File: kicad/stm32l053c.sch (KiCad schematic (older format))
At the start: 29 parts, among them P1 SWD, SW1 SW_PUSH, SW2 SW_PUSH, SW3 SW_PUSH, U1 STM32L053C8_LQFP48, U2 TLV61225, Y1 Crystal

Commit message: Some footprints
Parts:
- C10, C11, C5: footprint (none) -> Capacitors_SMD:C_0805_HandSoldering
- C8, C9: footprint Capacitors_SMD:C_0805_HandSoldering -> Capacitors_SMD:C_0603_HandSoldering
- L1: footprint (none) -> Inductors:Inductor_1212
- LS1: renamed from LS?; footprint (none) -> Resistors_SMD:R_0805_HandSoldering
- P1: footprint Pin_Headers:Pin_Header_Straight_1x06 -> Pin_Headers:Pin_Header_Straight_1x05
- Q1: renamed from Q?; footprint (none) -> TO_SOT_Packages_SMD:SOT-23_Handsoldering
- R3, R4, R5: footprint (none) -> Resistors_SMD:R_0805_HandSoldering
- R6: renamed from R?; footprint (none) -> Resistors_SMD:R_0805_HandSoldering
- U2: footprint (none) -> TO_SOT_Packages_SMD:SC-70-6
- Y1: footprint (none) -> Crystals:ABM3
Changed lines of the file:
@@
 $EndDescr
 $Comp
-L Earth #PWR24
+L Earth #PWR26
 U 1 1 58021BE1
 P 4900 7200
-F 0 "#PWR24" H 4900 6950 50  0001 C CNN
+F 0 "#PWR26" H 4900 6950 50  0001 C CNN
 F 1 "Earth" H 4900 7050 50  0001 C CNN
 F 2 "" H 4900 7200 50  0000 C CNN
@@
 $EndComp
 $Comp
-L VDD #PWR22
+L VDD #PWR24
 U 1 1 58021C2A
 P 4900 6900
-F 0 "#PWR22" H 4900 6750 50  0001 C CNN
+F 0 "#PWR24" H 4900 6750 50  0001 C CNN
 F 1 "VDD" H 4900 7050 50  0000 C CNN
 F 2 "" H 4900 6900 50  0000 C CNN
@@
 $EndComp
 $Comp
-L GNDA #PWR16
+L GNDA #PWR18
 U 1 1 58021F75
 P 5100 6300
-F 0 "#PWR16" H 5100 6050 50  0001 C CNN
+F 0 "#PWR18" H 5100 6050 50  0001 C CNN
 F 1 "GNDA" H 5100 6150 50  0000 C CNN
 F 2 "" H 5100 6300 50  0000 C CNN
@@
 $EndComp
 $Comp
-L Earth #PWR17
+L Earth #PWR19
 U 1 1 58021F89
 P 5600 6300
-F 0 "#PWR17" H 5600 6050 50  0001 C CNN
+F 0 "#PWR19" H 5600 6050 50  0001 C CNN
 F 1 "Earth" H 5600 6150 50  0001 C CNN
 F 2 "" H 5600 6300 50  0000 C CNN
@@
 $EndComp
 $Comp
-L GNDA #PWR14
+L GNDA #PWR15
 U 1 1 58022154
 P 5150 5800
-F 0 "#PWR14" H 5150 5550 50  0001 C CNN
+F 0 "#PWR15" H 5150 5550 50  0001 C CNN
 F 1 "GNDA" H 5150 5650 50  0000 C CNN
 F 2 "" H 5150 5800 50  0000 C CNN
@@
 $EndComp
 $Comp
-L Earth #PWR15
+L Earth #PWR16
 U 1 1 580221FA
 P 5650 5800
-F 0 "#PWR15" H 5650 5550 50  0001 C CNN
+F 0 "#PWR16" H 5650 5550 50  0001 C CNN
 F 1 "Earth" H 5650 5650 50  0001 C CNN
 F 2 "" H 5650 5800 50  0000 C CNN
@@
 F 0 "P1" H 1450 1750 50  0000 C CNN
 F 1 "SWD" V 1550 1400 50  0000 C CNN
-F 2 "Pin_Headers:Pin_Header_Straight_1x06" H 1450 1400 50  0001 C CNN
+F 2 "Pin_Headers:Pin_Header_Straight_1x05" H 1450 1400 50  0001 C CNN
 F 3 "" H 1450 1400 50  0000 C CNN
 	1    1450 1400
@@
 $EndComp
 $Comp
-L Earth #PWR25
+L Earth #PWR27
 U 1 1 5803BDC8
 P 5950 7200
-F 0 "#PWR25" H 5950 6950 50  0001 C CNN
+F 0 "#PWR27" H 5950 6950 50  0001 C CNN
 F 1 "Earth" H 5950 7050 50  0001 C CNN
 F 2 "" H 5950 7200 50  0000 C CNN
@@
 $EndComp
 $Comp
-L Earth #PWR12
+L Earth #PWR13
 U 1 1 58065816
 P 6550 5400
-F 0 "#PWR12" H 6550 5150 50  0001 C CNN
+F 0 "#PWR13" H 6550 5150 50  0001 C CNN
 F 1 "Earth" H 6550 5250 50  0001 C CNN
 F 2 "" H 6550 5400 50  0000 C CNN
@@
 $EndComp
 $Comp
-L Earth #PWR13
+L Earth #PWR14
 U 1 1 5806680D
 P 3600 5700
-F 0 "#PWR13" H 3600 5450 50  0001 C CNN
+F 0 "#PWR14" H 3600 5450 50  0001 C CNN
 F 1 "Earth" H 3600 5550 50  0001 C CNN
 F 2 "" H 3600 5700 50  0000 C CNN
@@
 F 0 "Y1" H 3600 5200 50  0000 C CNN
 F 1 "Crystal" H 3600 4900 50  0000 C CNN
-F 2 "" H 3600 5050 50  0000 C CNN
+F 2 "Crystals:ABM3" H 3600 5050 50  0001 C CNN
 F 3 "" H 3600 5050 50  0000 C CNN
 	1    3600 5050
@@
 F 0 "DS1" V 9500 4200 60  0000 C CNN
 F 1 "LCD_KITCHEN_TIMER" H 9500 4050 60  0000 C CNN
-F 2 "" H 9500 3950 60  0000 C CNN
+F 2 "" H 9500 3950 60  0001 C CNN
 F 3 "" H 9500 3950 60  0000 C CNN
 	1    9500 3950
@@
 F 0 "U2" H 2150 6650 60  0000 C CNN
 F 1 "TLV61225" H 2150 5950 60  0000 C CNN
-F 2 "" H 2150 6550 60  0001 C CNN
+F 2 "TO_SOT_Packages_SMD:SC-70-6" H 2150 6550 60  0001 C CNN
 F 3 "" H 2150 6550 60  0001 C CNN
 	1    2150 6500
@@
 F 0 "L1" V 1350 6550 50  0000 C CNN
 F 1 "INDUCTOR" V 1500 6550 50  0000 C CNN
-F 2 "" H 1400 6550 50  0000 C CNN
+F 2 "Inductors:Inductor_1212" H 1400 6550 50  0001 C CNN
 F 3 "" H 1400 6550 50  0000 C CNN
 	1    1400 6550
@@
 $EndComp
 $Comp
-L +BATT #PWR19
+L +BATT #PWR21
 U 1 1 584F2368
 P 850 6750
-F 0 "#PWR19" H 850 6600 50  0001 C CNN
+F 0 "#PWR21" H 850 6600 50  0001 C CNN
 F 1 "+BATT" H 850 6890 50  0000 C CNN
 F 2 "" H 850 6750 50  0000 C CNN
@@
 F 0 "C9" H 1275 7000 50  0000 L CNN
 F 1 "10uF" H 1275 6800 50  0000 L CNN
-F 2 "Capacitors_SMD:C_0805_HandSoldering" H 1288 6750 50  0001 C CNN
+F 2 "Capacitors_SMD:C_0603_HandSoldering" H 1288 6750 50  0001 C CNN
 F 3 "" H 1250 6900 50  0000 C CNN
 	1    1250 6900
@@
 F 0 "C8" H 2875 6800 50  0000 L CNN
 F 1 "10uF" H 2875 6600 50  0000 L CNN
-F 2 "Capacitors_SMD:C_0805_HandSoldering" H 2888 6550 50  0001 C CNN
+F 2 "Capacitors_SMD:C_0603_HandSoldering" H 2888 6550 50  0001 C CNN
 F 3 "" H 2850 6700 50  0000 C CNN
 	1    2850 6700
@@
 Connection ~ 2700 6550
 $Comp
-L Earth #PWR21
+L Earth #PWR23
 U 1 1 584F287E
 P 2850 6850
-F 0 "#PWR21" H 2850 6600 50  0001 C CNN
+F 0 "#PWR23" H 2850 6600 50  0001 C CNN
 F 1 "Earth" H 2850 6700 50  0001 C CNN
 F 2 "" H 2850 6850 50  0000 C CNN
@@
 $EndComp
 $Comp
-L Earth #PWR20
+L Earth #PWR22
 U 1 1 584F28E3
 P 1700 6850
-F 0 "#PWR20" H 1700 6600 50  0001 C CNN
+F 0 "#PWR22" H 1700 6600 50  0001 C CNN
 F 1 "Earth" H 1700 6700 50  0001 C CNN
 F 2 "" H 1700 6850 50  0000 C CNN
@@
 $EndComp
 $Comp
-L Earth #PWR23
+L Earth #PWR25
 U 1 1 584F2924
 P 1250 7050
-F 0 "#PWR23" H 1250 6800 50  0001 C CNN
+F 0 "#PWR25" H 1250 6800 50  0001 C CNN
 F 1 "Earth" H 1250 6900 50  0001 C CNN
 F 2 "" H 1250 7050 50  0000 C CNN
@@
 $EndComp
 $Comp
-L VDD #PWR18
+L VDD #PWR20
 U 1 1 584F2A51
 P 3200 6550
-F 0 "#PWR18" H 3200 6400 50  0001 C CNN
+F 0 "#PWR20" H 3200 6400 50  0001 C CNN
 F 1 "VDD" H 3200 6700 50  0000 C CNN
 F 2 "" H 3200 6550 50  0000 C CNN
@@
 F 0 "SW1" H 1850 2960 50  0000 C CNN
 F 1 "SW_PUSH" H 1700 2770 50  0000 C CNN
-F 2 "" H 1700 2850 50  0000 C CNN
+F 2 "" H 1700 2850 50  0001 C CNN
 F 3 "" H 1700 2850 50  0000 C CNN
 	1    1700 2850
@@
 F 0 "SW2" H 1850 3560 50  0000 C CNN
 F 1 "SW_PUSH" H 1700 3370 50  0000 C CNN
-F 2 "" H 1700 3450 50  0000 C CNN
+F 2 "" H 1700 3450 50  0001 C CNN
 F 3 "" H 1700 3450 50  0000 C CNN
 	1    1700 3450
@@
 F 0 "SW3" H 1850 4160 50  0000 C CNN
 F 1 "SW_PUSH" H 1700 3970 50  0000 C CNN
-F 2 "" H 1700 4050 50  0000 C CNN
+F 2 "" H 1700 4050 50  0001 C CNN
 F 3 "" H 1700 4050 50  0000 C CNN
 	1    1700 4050
@@
 F 0 "R3" V 2380 2850 50  0000 C CNN
 F 1 "1K" V 2300 2850 50  0000 C CNN
-F 2 "" V 2230 2850 50  0000 C CNN
+F 2 "Resistors_SMD:R_0805_HandSoldering" V 2230 2850 50  0001 C CNN
 F 3 "" H 2300 2850 50  0000 C CNN
 	1    2300 2850
@@
 F 0 "R4" V 2380 3450 50  0000 C CNN
 F 1 "1K" V 2300 3450 50  0000 C CNN
-F 2 "" V 2230 3450 50  0000 C CNN
+F 2 "Resistors_SMD:R_0805_HandSoldering" V 2230 3450 50  0001 C CNN
 F 3 "" H 2300 3450 50  0000 C CNN
 	1    2300 3450
@@
 F 0 "R5" V 2380 4050 50  0000 C CNN
 F 1 "1K" V 2300 4050 50  0000 C CNN
-F 2 "" V 2230 4050 50  0000 C CNN
+F 2 "Resistors_SMD:R_0805_HandSoldering" V 2230 4050 50  0001 C CNN
 F 3 "" H 2300 4050 50  0000 C CNN
 	1    2300 4050
@@
 F 0 "C5" H 2475 3100 50  0000 L CNN
 F 1 "100nF" H 2475 2900 50  0000 L CNN
-F 2 "" H 2488 2850 50  0000 C CNN
+F 2 "Capacitors_SMD:C_0805_HandSoldering" H 2488 2850 50  0001 C CNN
 F 3 "" H 2450 3000 50  0000 C CNN
 	1    2450 3000
@@
 F 0 "C10" H 2475 3700 50  0000 L CNN
 F 1 "100nF" H 2475 3500 50  0000 L CNN
-F 2 "" H 2488 3450 50  0000 C CNN
+F 2 "Capacitors_SMD:C_0805_HandSoldering" H 2488 3450 50  0001 C CNN
 F 3 "" H 2450 3600 50  0000 C CNN
 	1    2450 3600
@@
 F 0 "C11" H 2475 4300 50  0000 L CNN
 F 1 "100nF" H 2475 4100 50  0000 L CNN
-F 2 "" H 2488 4050 50  0000 C CNN
+F 2 "Capacitors_SMD:C_0805_HandSoldering" H 2488 4050 50  0001 C CNN
 F 3 "" H 2450 4200 50  0000 C CNN
 	1    2450 4200
@@
 $EndComp
 $Comp
-L BUZZER LS?
+L BUZZER LS1
 U 1 1 5851ABB3
 P 9500 5200
-F 0 "LS?" H 9500 5450 60  0000 C CNN
+F 0 "LS1" H 9500 5450 60  0000 C CNN
 F 1 "BUZZER" H 9500 4950 60  0000 C CNN
-F 2 "" H 9650 5450 60  0001 C CNN
+F 2 "Resistors_SMD:R_0805_HandSoldering" H 9650 5450 60  0001 C CNN
 F 3 "" H 9650 5450 60  0001 C CNN
 	1    9500 5200
@@
 $EndComp
 $Comp
-L Q_NPN_CBE Q?
+L Q_NPN_CBE Q1
 U 1 1 5851AC3A
 P 9200 5650
-F 0 "Q?" H 9500 5700 50  0000 R CNN
+F 0 "Q1" H 9500 5700 50  0000 R CNN
 F 1 "Q_NPN_CBE" H 9800 5600 50  0000 R CNN
-F 2 "" H 9400 5750 50  0000 C CNN
+F 2 "TO_SOT_Packages_SMD:SOT-23_Handsoldering" H 9400 5750 50  0001 C CNN
 F 3 "" H 9200 5650 50  0000 C CNN
 	1    9200 5650
@@
 $EndComp
 $Comp
-L R R?
+L R R6
 U 1 1 5851ADE5
 P 8750 5650
-F 0 "R?" V 8830 5650 50  0000 C CNN
+F 0 "R6" V 8830 5650 50  0000 C CNN
 F 1 "1K" V 8750 5650 50  0000 C CNN
-F 2 "" V 8680 5650 50  0000 C CNN
+F 2 "Resistors_SMD:R_0805_HandSoldering" V 8680 5650 50  0001 C CNN
 F 3 "" H 8750 5650 50  0000 C CNN
 	1    8750 5650
@@
 	8600 5650 8200 5650
 $Comp
-L Earth #PWR?
+L Earth #PWR17
 U 1 1 5851B22D
 P 9300 5850
-F 0 "#PWR?" H 9300 5600 50  0001 C CNN
+F 0 "#PWR17" H 9300 5600 50  0001 C CNN
 F 1 "Earth" H 9300 5700 50  0001 C CNN
 F 2 "" H 9300 5850 50  0000 C CNN
@@
 $EndComp
 $Comp
-L VDD #PWR?
+L VDD #PWR12
 U 1 1 5851B377
 P 9300 5150
-F 0 "#PWR?" H 9300 5000 50  0001 C CNN
+F 0 "#PWR12" H 9300 5000 50  0001 C CNN
 F 1 "VDD" H 9300 5300 50  0000 C CNN
 F 2 "" H 9300 5150 50  0000 C CNN

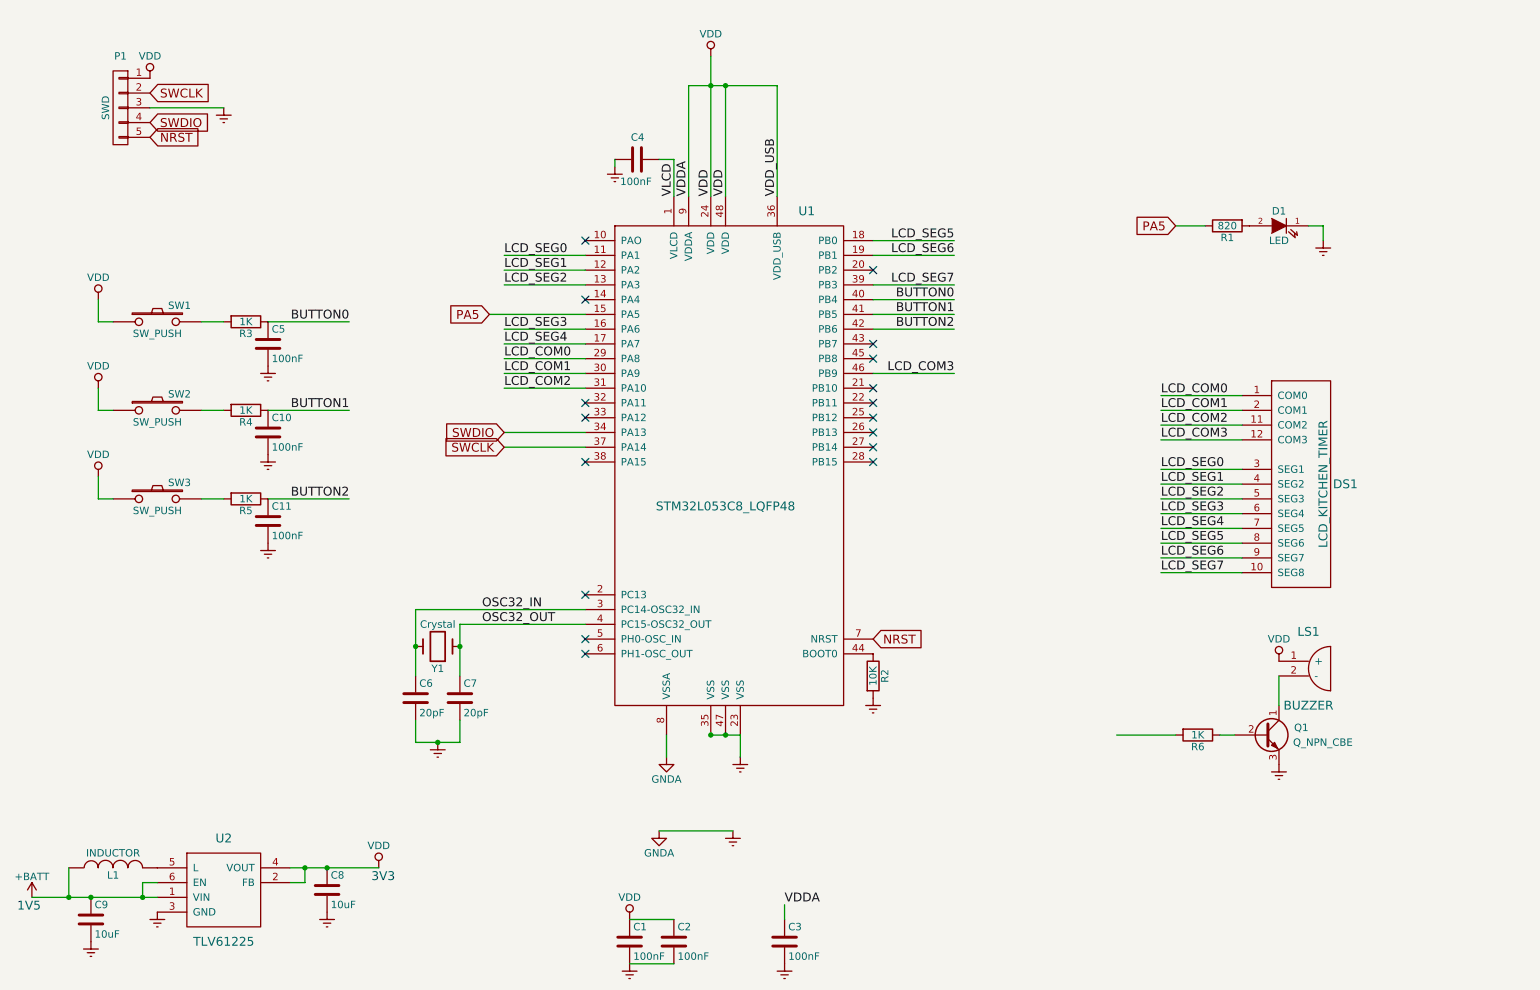
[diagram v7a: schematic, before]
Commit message: Mosfet to drive the buzzer
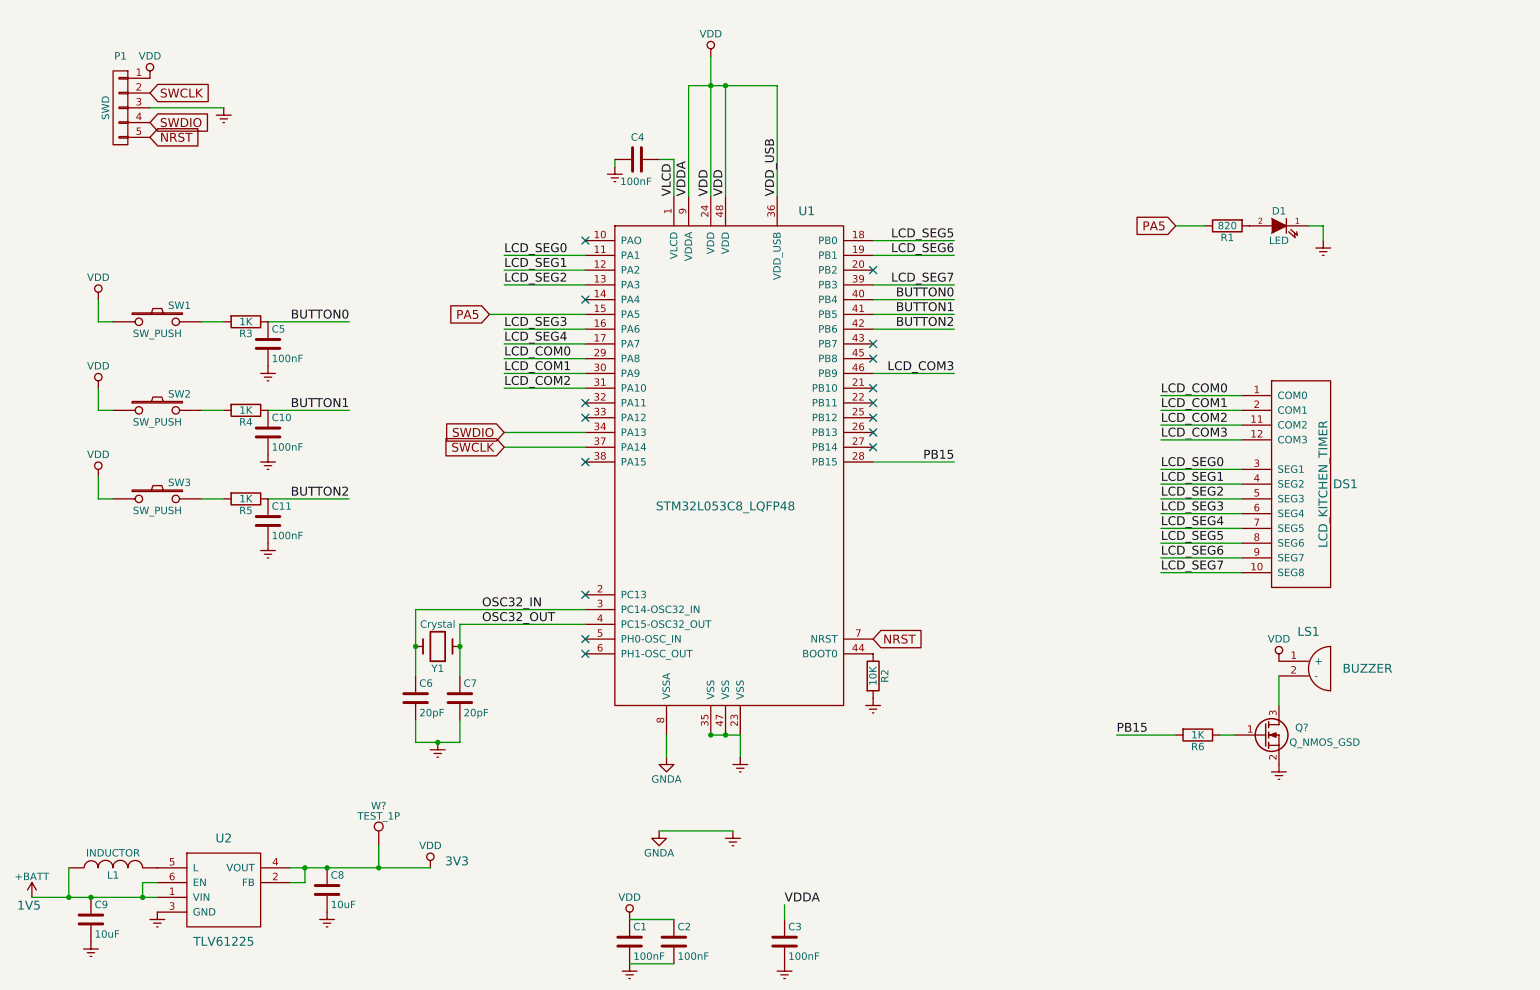
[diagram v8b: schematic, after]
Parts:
- removed Q1: Q_NPN_CBE, TO_SOT_Packages_SMD:SOT-23_Handsoldering, symbol Q_NPN_CBE
- added Q?: Q_NMOS_GSD, symbol Q_NMOS_GSD
- added W?: TEST_1P, symbol TEST_1P
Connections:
- net Earth: now also Q?.2 (S)
- net VDD: now also W?.1
- net PB15: now reaches U1.28 (PB15)
- net PB15: now also R6.2
- net at LS1.2 (-): now also Q?.3 (D)
- net at R6.1: now also Q?.1 (G)
- no-connect marks 17 -> 16
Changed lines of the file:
@@
 NoConn ~ 6550 3600
 NoConn ~ 6550 3700
-NoConn ~ 6550 3800
 NoConn ~ 4600 2300
 NoConn ~ 4600 2700
@@
 Connection ~ 1600 6750
 Wire Wire Line
-	2600 6550 3200 6550
+	2600 6550 3550 6550
 Connection ~ 2850 6550
 Wire Wire Line
@@
 L VDD #PWR20
 U 1 1 584F2A51
-P 3200 6550
-F 0 "#PWR20" H 3200 6400 50  0001 C CNN
-F 1 "VDD" H 3200 6700 50  0000 C CNN
-F 2 "" H 3200 6550 50  0000 C CNN
-F 3 "" H 3200 6550 50  0000 C CNN
-	1    3200 6550
-	1    0    0    -1
-$EndComp
-Text Notes 3150 6650 0    60   ~ 0
+P 3550 6550
+F 0 "#PWR20" H 3550 6400 50  0001 C CNN
+F 1 "VDD" H 3550 6700 50  0000 C CNN
+F 2 "" H 3550 6550 50  0000 C CNN
+F 3 "" H 3550 6550 50  0000 C CNN
+	1    3550 6550
+	1    0    0    -1
+$EndComp
+Text Notes 3650 6550 0    60   ~ 0
 3V3
 Text Notes 750  6850 0    60   ~ 0
@@
 P 9500 5200
 F 0 "LS1" H 9500 5450 60  0000 C CNN
-F 1 "BUZZER" H 9500 4950 60  0000 C CNN
+F 1 "BUZZER" H 9900 5200 60  0000 C CNN
 F 2 "Resistors_SMD:R_0805_HandSoldering" H 9650 5450 60  0001 C CNN
 F 3 "" H 9650 5450 60  0001 C CNN
 	1    9500 5200
-	1    0    0    -1
-$EndComp
-$Comp
-L Q_NPN_CBE Q1
-U 1 1 5851AC3A
-P 9200 5650
-F 0 "Q1" H 9500 5700 50  0000 R CNN
-F 1 "Q_NPN_CBE" H 9800 5600 50  0000 R CNN
-F 2 "TO_SOT_Packages_SMD:SOT-23_Handsoldering" H 9400 5750 50  0001 C CNN
-F 3 "" H 9200 5650 50  0000 C CNN
-	1    9200 5650
 	1    0    0    -1
 $EndComp
@@
 	1    0    0    -1
 $EndComp
+$Comp
+L TEST_1P W?
+U 1 1 58557FAC
+P 3200 6400
+F 0 "W?" H 3200 6670 50  0000 C CNN
+F 1 "TEST_1P" H 3200 6600 50  0000 C CNN
+F 2 "" H 3400 6400 50  0000 C CNN
+F 3 "" H 3400 6400 50  0000 C CNN
+	1    3200 6400
+	1    0    0    -1
+$EndComp
+Wire Wire Line
+	3200 6400 3200 6550
+Connection ~ 3200 6550
+$Comp
+L Q_NMOS_GSD Q?
+U 1 1 585590EB
+P 9200 5650
+F 0 "Q?" H 9500 5700 50  0000 R CNN
+F 1 "Q_NMOS_GSD" H 9850 5600 50  0000 R CNN
+F 2 "" H 9400 5750 50  0000 C CNN
+F 3 "" H 9200 5650 50  0000 C CNN
+	1    9200 5650
+	1    0    0    -1
+$EndComp
+Text Label 7100 3800 2    60   ~ 0
+PB15
+Wire Wire Line
+	6550 3800 7100 3800
+Text Label 8200 5650 0    60   ~ 0
+PB15
 $EndSCHEMATC
